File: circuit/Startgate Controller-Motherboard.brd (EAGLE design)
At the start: 160 x 100 mm, 25 parts, among them IC1 MAX3490ESA, IC2 L293D, U2 HEF4066BT, U3 HEF4066BT, U4 HEF4066BT, U5 HEF4066BT, X1 RJ45-8L21-B, X2 SOLENOID

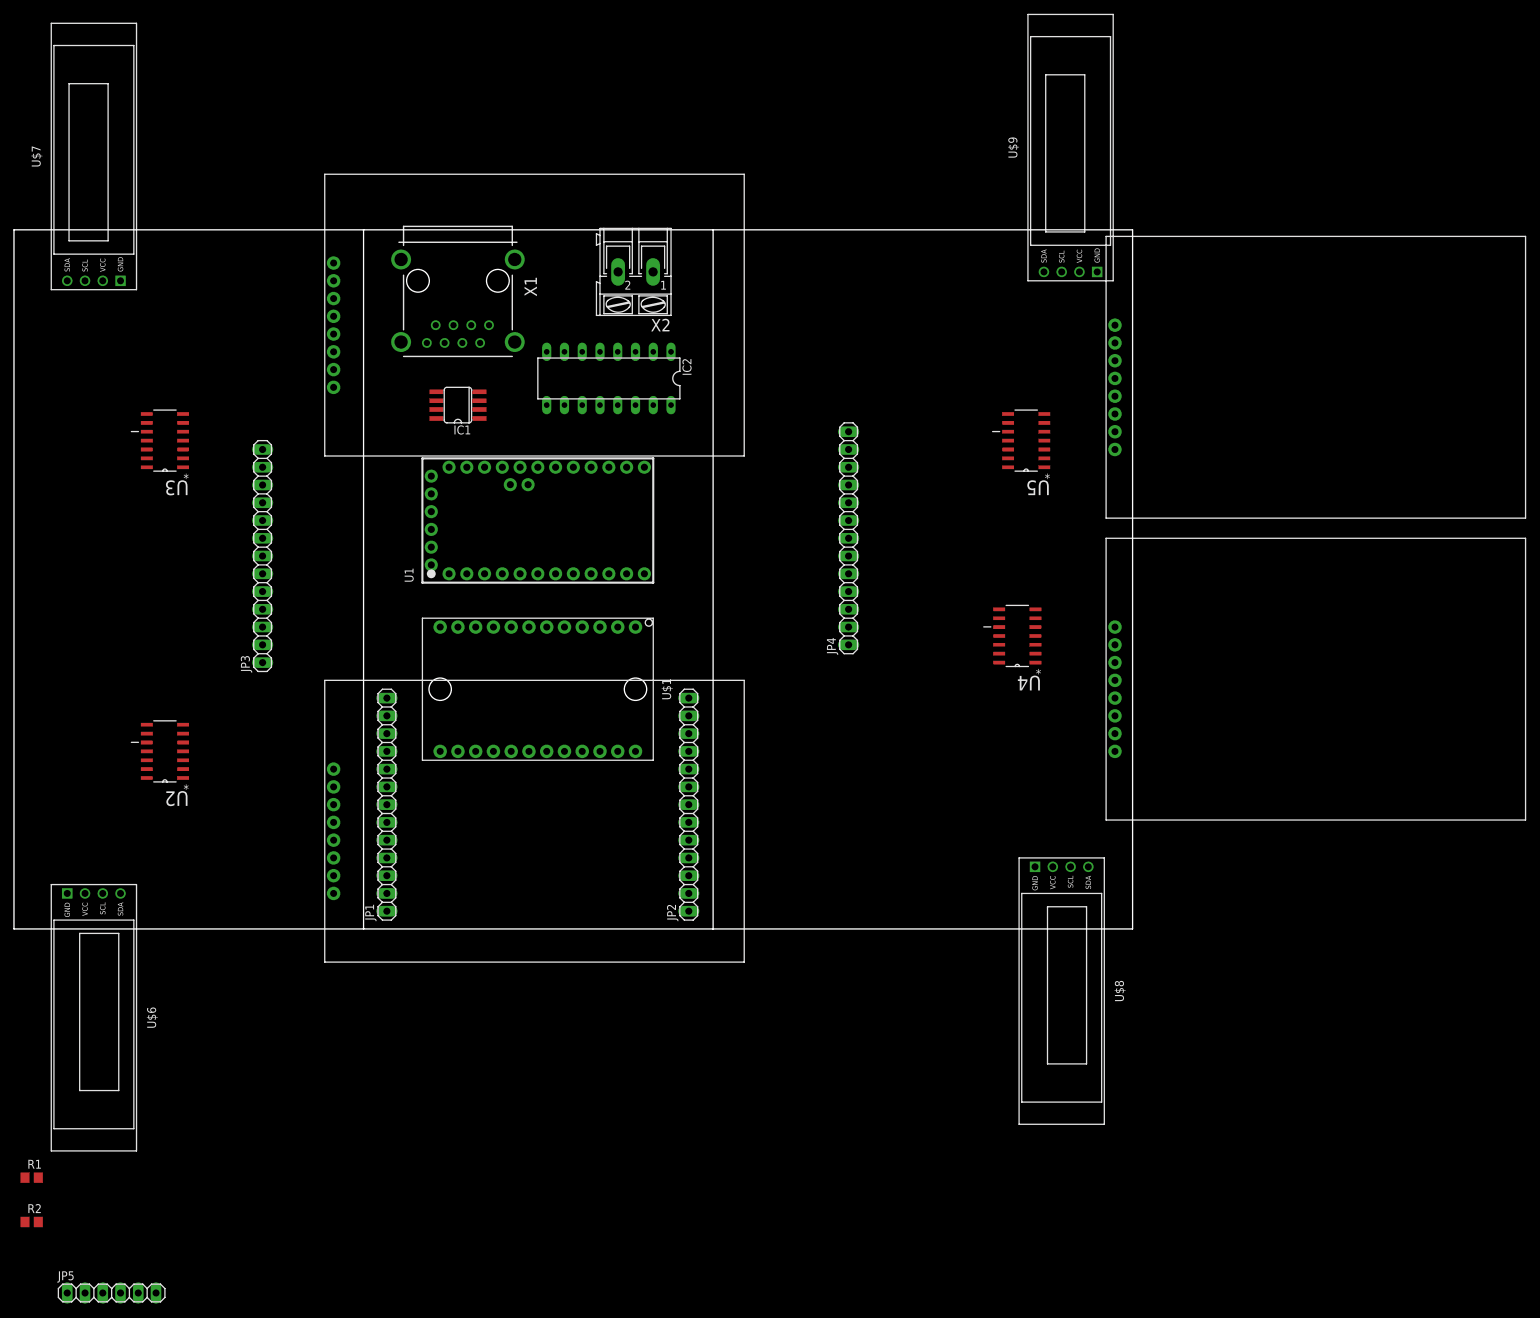
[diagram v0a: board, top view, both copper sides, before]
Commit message: correct some schematics mistakes and add gerber files
A demo mode button was added to the controller, the layout of the
controller shield as well as the startgate displays were changed.
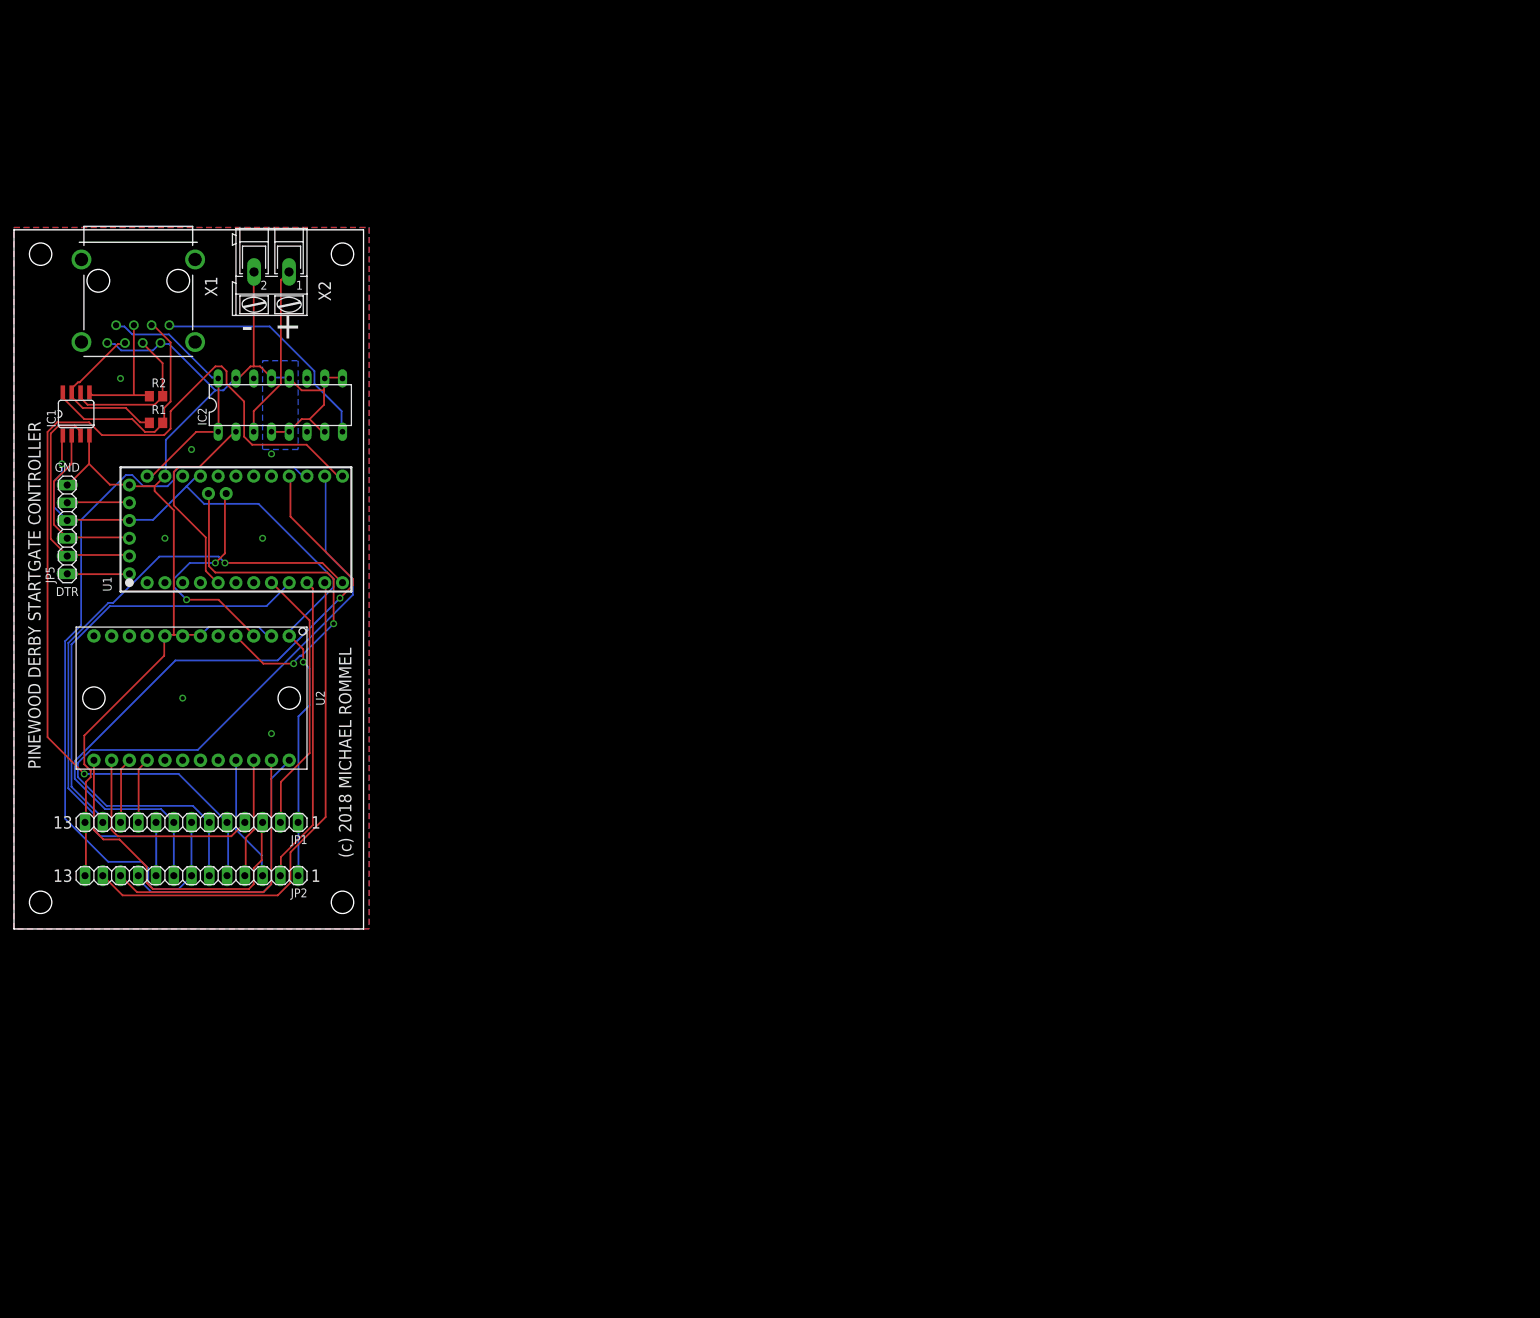
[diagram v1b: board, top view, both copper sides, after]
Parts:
- removed JP3, JP4: (no value), pinhead:1X13
- removed U$1: TCA9548A, miro:DIL24
- removed U$2, U$3, U$4, U$5: RFID-RC522, miro:RFID-RC522
- removed U$6, U$7, U$8, U$9: DISPLAY-OLED-128X32, diy-modules:DISPLAY-OLED-128X32
- removed U3, U4, U5: HEF4066BT, NXP_By_element14_Batch_1:SOIC127P600X175-14N
- JP1: value (none) -> LEFT
- JP2: value (none) -> RIGHT
- JP5: value (none) -> FTDI
- R1, R2: value (none) -> 120
- U1: value (none) -> PROMINI
- U2: value HEF4066BT -> TCA9548A; device NXP_By_element14_Batch_1:SOIC127P600X175-14N -> miro:DIL24
- moved R2 119.4 mm to (20.3, 76.2)
- moved R1 109.4 mm to (20.3, 72.4)
- moved JP5 109.4 mm to (7.62, 57.1), turned to 90 degrees
- moved JP2 71.8 mm to (25.4, 7.62), turned to 180 degrees
- moved IC1 54.6 mm to (8.89, 73.7), turned to 0 degrees
- moved X2 52.1 mm to (36.8, 94.0)
- moved IC2 47.1 mm to (38.1, 74.9), turned to 0 degrees
- moved X1 45.7 mm to (17.8, 92.7)
- moved U1 43.2 mm to (48.3, 48.3)
- moved JP1 28.1 mm to (25.4, 15.2), turned to 180 degrees
- moved U2 21.8 mm to (8.89, 43.2), turned to 270 degrees
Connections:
- removed net MISO-OUT1: U$2.4, U2.10
- removed net MISO-OUT2: U$3.4, U3.10
- removed net MISO-OUT3: U$4.4, U4.10
- removed net MISO-OUT4: U$5.4, U5.10
- removed net MOSI-OUT1: U$2.3, U2.9
- removed net MOSI-OUT2: U$3.3, U3.9
- removed net MOSI-OUT3: U$4.3, U4.9
- removed net MOSI-OUT4: U$5.3, U5.9
- removed net N$13: IC2.12, IC2.13, IC2.4, IC2.5, X1.2, X1.8, X2.2
- removed net SCK-OUT1: U$2.2, U2.3
- removed net SCK-OUT2: U$3.2, U3.3
- removed net SCK-OUT3: U$4.2, U4.3
- removed net SCK-OUT4: U$5.2, U5.3
- removed net SS-OUT1: U$2.1, U2.2
- removed net SS-OUT2: U$3.1, U3.2
- removed net SS-OUT3: U$4.1, U4.2
- removed net SS-OUT4: U$5.1, U5.2
- removed net VCC2: IC2.8
- net +12V: now also IC2.8
- net +3V3: now also U2.1; no longer JP3.1, JP4.1, U$1.1, U$2.8, U$3.8, U$4.8, U$5.8, U$6.2, U$7.2, U$8.2, U$9.2, U2.14, U3.14, U4.14, U5.14
- net +5V: now also IC2.1
- net ENA1: no longer JP3.2, U2.12, U2.13, U2.5, U2.6
- net ENA2: no longer JP3.12, U3.12, U3.13, U3.5, U3.6
- net ENA3: no longer JP4.2, U4.12, U4.13, U4.5, U4.6
- net ENA4: no longer JP4.12, U5.12, U5.13, U5.5, U5.6
- net GND: now also IC2.10, IC2.12, IC2.13, IC2.15, IC2.4, IC2.5, IC2.7, IC2.9, U2.2, U2.6, U2.8, X1.2, X1.8, X2.2; no longer JP3.13, JP4.13, U$1.2, U$1.6, U$1.7, U$1.8, U$2.6, U$3.6, U$4.6, U$5.6, U$6.1, U$7.1, U$8.1, U$9.1, U3.7, U4.7, U5.7
- net MISO: no longer JP3.7, JP4.7, U2.11, U3.11, U4.11, U5.11
- net MOSI: no longer JP3.6, JP4.6, U2.8, U3.8, U4.8, U5.8
- net N$5: now also U2.4; no longer U$1.4
- net N$6: now also U2.3; no longer U$1.3
- net RST: no longer JP3.9, JP4.9, U$2.7, U$3.7, U$4.7, U$5.7
- net SCK: no longer JP3.8, JP4.8, U2.4, U3.4, U4.4, U5.4
- net SCL1: now also U2.14; no longer JP3.4, U$1.14, U$6.3
- net SCL2: now also U2.16; no longer JP3.10, U$1.16, U$7.3
- net SCL3: now also U2.22; no longer JP4.4, U$1.22, U$8.3
- net SCL4: now also U2.24; no longer JP4.10, U$1.24, U$9.3
- net SDA1: now also U2.13; no longer JP3.3, U$1.13, U$6.4
- net SDA2: now also U2.15; no longer JP3.11, U$1.15, U$7.4
- net SDA3: now also U2.21; no longer JP4.3, U$1.21, U$8.4
- net SDA4: now also U2.23; no longer JP4.11, U$1.23, U$9.4
- net SS: no longer JP3.5, JP4.5, U2.1, U3.1, U4.1, U5.1
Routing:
- net GND: track 0.00 -> 185.3 mm, vias 0 -> 7
- net SS: track 0.00 -> 141.7 mm, vias 0 -> 1
- net MISO: track 0.00 -> 113.7 mm
- net +3V3: track 0.00 -> 108.8 mm, vias 0 -> 2
- net MOSI: track 0.00 -> 99.1 mm
- net SCK: track 0.00 -> 96.6 mm, vias 0 -> 1
- net RST: track 0.00 -> 91.0 mm, vias 0 -> 1
- net ENA4: track 0.00 -> 73.8 mm
- net ENA2: track 0.00 -> 62.2 mm
- net N$5: track 0.00 -> 53.5 mm, vias 0 -> 2
- net SDA1: track 0.00 -> 47.3 mm
- net ENA3: track 0.00 -> 44.2 mm
- net SDA4: track 0.00 -> 40.7 mm
- net SCL4: track 0.00 -> 39.5 mm
- net ENA1: track 0.00 -> 38.3 mm
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- added copper zone on layer 1, net GND
- added copper zone on layer 16, net GND
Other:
- board size 160 x 100 mm -> 50 x 100 mm
- board text added: "(c) 2018 MICHAEL ROMMEL"
- board text added: "- +"
- board text added: "1"
- board text added: "13"
- board text added: "DTR"
- board text added: "GND"
- board text added: "PINEWOOD DERBY STARTGATE CONTROLLER"
